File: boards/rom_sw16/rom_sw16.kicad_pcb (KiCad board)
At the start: 2 copper layers, 99.1 x 99.1 mm, 95 parts, among them J1 Conn_02x10_Top_Bottom, SW1 SW_DIP_x08, SW10 SW_DIP_x08, SW11 SW_DIP_x08, SW12 SW_DIP_x08, SW13 SW_DIP_x08, SW14 SW_DIP_x08, SW15 SW_DIP_x08, SW16 SW_DIP_x08, SW2 SW_DIP_x08, SW3 SW_DIP_x08, SW4 SW_DIP_x08, SW5 SW_DIP_x08, SW6 SW_DIP_x08, SW7 SW_DIP_x08, SW8 SW_DIP_x08, SW9 SW_DIP_x08, U1 74HC138, U2 74HC138, U3 74HC240

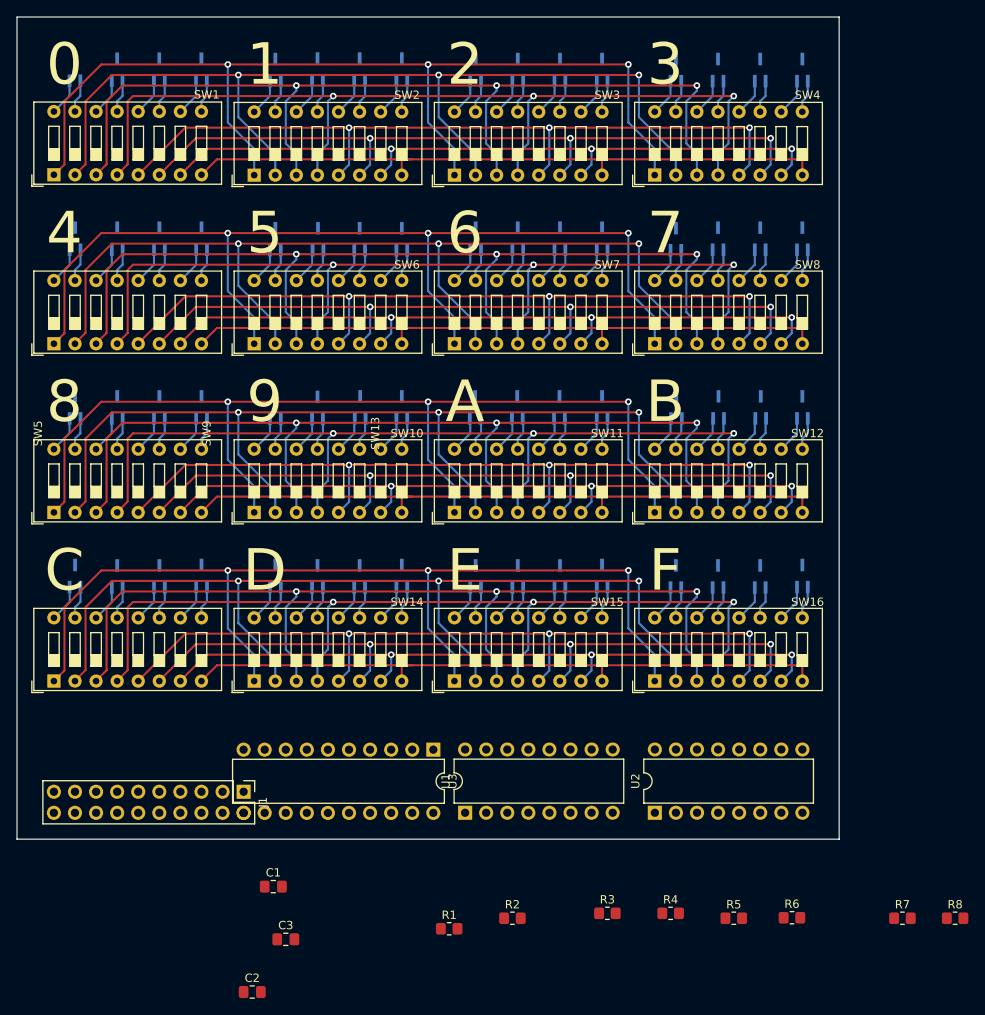
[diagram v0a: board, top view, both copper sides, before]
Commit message: rom_sw16: add board design
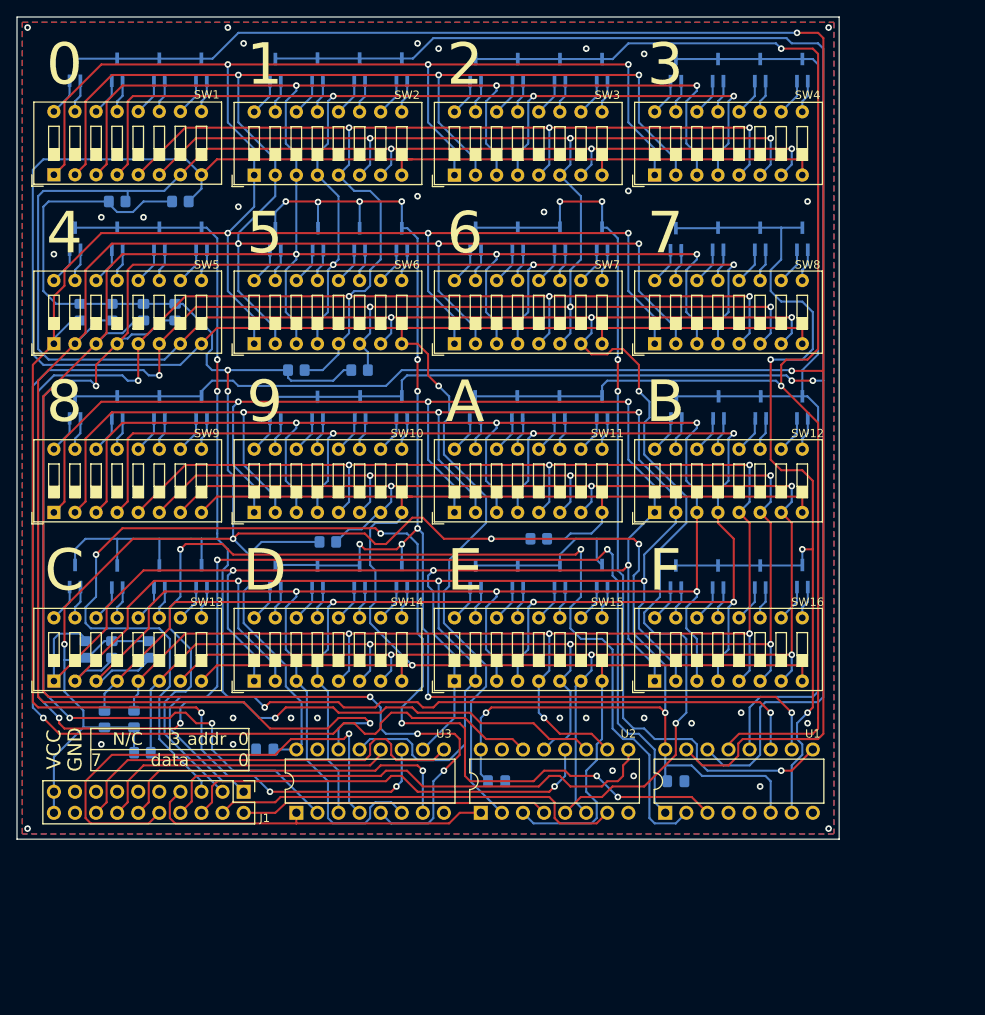
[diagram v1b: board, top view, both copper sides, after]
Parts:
- added R1: 10k, Resistor_SMD:R_0805_2012Metric_Pad1.20x1.40mm_HandSolder, B.Cu at (66.0, 43.8)
- added R10: 10k, Resistor_SMD:R_0805_2012Metric_Pad1.20x1.40mm_HandSolder, B.Cu at (83.8, 84.8)
- added R11: 10k, Resistor_SMD:R_0805_2012Metric_Pad1.20x1.40mm_HandSolder, B.Cu at (61.5, 110.2)
- added R12: 10k, Resistor_SMD:R_0805_2012Metric_Pad1.20x1.40mm_HandSolder, B.Cu at (60.5, 106.2)
- added R2: 10k, Resistor_SMD:R_0805_2012Metric_Pad1.20x1.40mm_HandSolder, B.Cu at (58.4, 43.8)
- added R3: 10k, Resistor_SMD:R_0805_2012Metric_Pad1.20x1.40mm_HandSolder, B.Cu at (87.6, 64.1)
- added R4: 10k, Resistor_SMD:R_0805_2012Metric_Pad1.20x1.40mm_HandSolder, B.Cu at (80.0, 64.1)
- added R9: 10k, Resistor_SMD:R_0805_2012Metric_Pad1.20x1.40mm_HandSolder, B.Cu at (109.2, 84.5)
- C1, C2, C3: moved to B.Cu
- R13: renamed from R2; moved to B.Cu
- R14: renamed from R4; moved to B.Cu
- R15: renamed from R6; moved to B.Cu
- R16: renamed from R8; moved to B.Cu
- R5: renamed from R1; moved to B.Cu
- R6: renamed from R3; moved to B.Cu
- R7: renamed from R5; moved to B.Cu
- R8: renamed from R7; moved to B.Cu
- U2: value 74HC138 -> 74HC158
- U3: value 74HC240 -> 74HC158; footprint PrjLibrary_MainBoard:DIP-20_W7.62mm_D1mm -> PrjLibrary_MainBoard:DIP-16_W7.62mm_D1mm
- moved R8 123.1 mm to (54.0, 57.1), turned to -90 degrees
- moved R16 109.7 mm to (54.6, 97.8), turned to 90 degrees
- moved R7 104.6 mm to (57.8, 57.1), turned to -90 degrees
- moved R6 91.5 mm to (61.6, 57.1), turned to -90 degrees
- moved R15 88.1 mm to (57.8, 97.8), turned to -90 degrees
- moved R5 81.3 mm to (65.4, 57.1), turned to -90 degrees
- moved R14 70.5 mm to (62.2, 97.8), turned to -90 degrees
- moved R13 54.7 mm to (56.9, 106.2), turned to 90 degrees
- moved C1 50.1 mm to (125.7, 113.7)
- moved C2 38.9 mm to (104.1, 113.7)
- moved U1 24.1 mm to (124.5, 117.5)
- moved C3 23.0 mm to (76.2, 109.9), turned to 180 degrees
- moved U2 21.0 mm to (102.2, 117.5)
- moved U3 18.2 mm to (80.0, 117.5), turned to 90 degrees
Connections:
- D33 pad 3: /enB -> /en3
- D34 pad 3: /enB -> /en3
- D35 pad 3: /enB -> /en3
- D36 pad 3: /enB -> /en3
- D37 pad 3: /enA -> /en2
- D38 pad 3: /enA -> /en2
- D39 pad 3: /enA -> /en2
- D40 pad 3: /enA -> /en2
- D41 pad 3: /en9 -> /en1
- D42 pad 3: /en9 -> /en1
- D43 pad 3: /en9 -> /en1
- D44 pad 3: /en9 -> /en1
- D45 pad 3: /en8 -> /en0
- D46 pad 3: /en8 -> /en0
- D47 pad 3: /en8 -> /en0
- D48 pad 3: /en8 -> /en0
- D49 pad 3: /enF -> /en7
- D50 pad 3: /enF -> /en7
- D51 pad 3: /enF -> /en7
- D52 pad 3: /enF -> /en7
- D53 pad 3: /enE -> /en6
- D54 pad 3: /enE -> /en6
- D55 pad 3: /enE -> /en6
- D56 pad 3: /enE -> /en6
- D57 pad 3: /enD -> /en5
- D58 pad 3: /enD -> /en5
- D59 pad 3: /enD -> /en5
- D60 pad 3: /enD -> /en5
- D61 pad 3: /enC -> /en4
- D62 pad 3: /enC -> /en4
- D63 pad 3: /enC -> /en4
- D64 pad 3: /enC -> /en4
- R13 pad 2: /sw1 -> /sH4
- R14 pad 2: /sw3 -> /sH5
- R15 pad 2: /sw5 -> /sH6
- R16 pad 2: /sw7 -> /sH7
- R5 pad 2: /sw0 -> /sL4
- R6 pad 2: /sw2 -> /sL5
- R7 pad 2: /sw4 -> /sL6
- R8 pad 2: /sw6 -> /sL7
- SW1 pad 1: /sw7 -> /sL7
- SW1 pad 2: /sw6 -> /sL6
- SW1 pad 3: /sw5 -> /sL5
- SW1 pad 4: /sw4 -> /sL4
- SW1 pad 5: /sw3 -> /sL3
- SW1 pad 6: /sw2 -> /sL2
- SW1 pad 7: /sw1 -> /sL1
- SW1 pad 8: /sw0 -> /sL0
- SW10 pad 1: /sw7 -> /sH7
- SW10 pad 2: /sw6 -> /sH6
- SW10 pad 3: /sw5 -> /sH5
- SW10 pad 4: /sw4 -> /sH4
- SW10 pad 5: /sw3 -> /sH3
- SW10 pad 6: /sw2 -> /sH2
- SW10 pad 7: /sw1 -> /sH1
- SW10 pad 8: /sw0 -> /sH0
- SW11 pad 1: /sw7 -> /sH7
- SW11 pad 2: /sw6 -> /sH6
- SW11 pad 3: /sw5 -> /sH5
- SW11 pad 4: /sw4 -> /sH4
- SW11 pad 5: /sw3 -> /sH3
- SW11 pad 6: /sw2 -> /sH2
- SW11 pad 7: /sw1 -> /sH1
- SW11 pad 8: /sw0 -> /sH0
- SW12 pad 1: /sw7 -> /sH7
- SW12 pad 2: /sw6 -> /sH6
- SW12 pad 3: /sw5 -> /sH5
- SW12 pad 4: /sw4 -> /sH4
- SW12 pad 5: /sw3 -> /sH3
- SW12 pad 6: /sw2 -> /sH2
- SW12 pad 7: /sw1 -> /sH1
- SW12 pad 8: /sw0 -> /sH0
- SW13 pad 1: /sw7 -> /sH7
- SW13 pad 2: /sw6 -> /sH6
- SW13 pad 3: /sw5 -> /sH5
- SW13 pad 4: /sw4 -> /sH4
- SW13 pad 5: /sw3 -> /sH3
- SW13 pad 6: /sw2 -> /sH2
- SW13 pad 7: /sw1 -> /sH1
- SW13 pad 8: /sw0 -> /sH0
- SW14 pad 1: /sw7 -> /sH7
- SW14 pad 2: /sw6 -> /sH6
- SW14 pad 3: /sw5 -> /sH5
- SW14 pad 4: /sw4 -> /sH4
- SW14 pad 5: /sw3 -> /sH3
- SW14 pad 6: /sw2 -> /sH2
- SW14 pad 7: /sw1 -> /sH1
- SW14 pad 8: /sw0 -> /sH0
- SW15 pad 1: /sw7 -> /sH7
- SW15 pad 2: /sw6 -> /sH6
- SW15 pad 3: /sw5 -> /sH5
- SW15 pad 4: /sw4 -> /sH4
- SW15 pad 5: /sw3 -> /sH3
- SW15 pad 6: /sw2 -> /sH2
- SW15 pad 7: /sw1 -> /sH1
- SW15 pad 8: /sw0 -> /sH0
- SW16 pad 1: /sw7 -> /sH7
- SW16 pad 2: /sw6 -> /sH6
- SW16 pad 3: /sw5 -> /sH5
- SW16 pad 4: /sw4 -> /sH4
- SW16 pad 5: /sw3 -> /sH3
- SW16 pad 6: /sw2 -> /sH2
- SW16 pad 7: /sw1 -> /sH1
- SW16 pad 8: /sw0 -> /sH0
- SW2 pad 1: /sw7 -> /sL7
- SW2 pad 2: /sw6 -> /sL6
- SW2 pad 3: /sw5 -> /sL5
- SW2 pad 4: /sw4 -> /sL4
- SW2 pad 5: /sw3 -> /sL3
- SW2 pad 6: /sw2 -> /sL2
- SW2 pad 7: /sw1 -> /sL1
- SW2 pad 8: /sw0 -> /sL0
- SW3 pad 1: /sw7 -> /sL7
- SW3 pad 2: /sw6 -> /sL6
- SW3 pad 3: /sw5 -> /sL5
- SW3 pad 4: /sw4 -> /sL4
- SW3 pad 5: /sw3 -> /sL3
- SW3 pad 6: /sw2 -> /sL2
- SW3 pad 7: /sw1 -> /sL1
- SW3 pad 8: /sw0 -> /sL0
- SW4 pad 1: /sw7 -> /sL7
- SW4 pad 2: /sw6 -> /sL6
- SW4 pad 3: /sw5 -> /sL5
- SW4 pad 4: /sw4 -> /sL4
- SW4 pad 5: /sw3 -> /sL3
- SW4 pad 6: /sw2 -> /sL2
- SW4 pad 7: /sw1 -> /sL1
- SW4 pad 8: /sw0 -> /sL0
- SW5 pad 1: /sw7 -> /sL7
- SW5 pad 2: /sw6 -> /sL6
- SW5 pad 3: /sw5 -> /sL5
- SW5 pad 4: /sw4 -> /sL4
- SW5 pad 5: /sw3 -> /sL3
- SW5 pad 6: /sw2 -> /sL2
- SW5 pad 7: /sw1 -> /sL1
- SW5 pad 8: /sw0 -> /sL0
- SW6 pad 1: /sw7 -> /sL7
- SW6 pad 2: /sw6 -> /sL6
- SW6 pad 3: /sw5 -> /sL5
- SW6 pad 4: /sw4 -> /sL4
- SW6 pad 5: /sw3 -> /sL3
- SW6 pad 6: /sw2 -> /sL2
- SW6 pad 7: /sw1 -> /sL1
- SW6 pad 8: /sw0 -> /sL0
- SW7 pad 1: /sw7 -> /sL7
- SW7 pad 2: /sw6 -> /sL6
- SW7 pad 3: /sw5 -> /sL5
- SW7 pad 4: /sw4 -> /sL4
- SW7 pad 5: /sw3 -> /sL3
- SW7 pad 6: /sw2 -> /sL2
- SW7 pad 7: /sw1 -> /sL1
- SW7 pad 8: /sw0 -> /sL0
- SW8 pad 1: /sw7 -> /sL7
- SW8 pad 2: /sw6 -> /sL6
- SW8 pad 3: /sw5 -> /sL5
- SW8 pad 4: /sw4 -> /sL4
- SW8 pad 5: /sw3 -> /sL3
- SW8 pad 6: /sw2 -> /sL2
- SW8 pad 7: /sw1 -> /sL1
- SW8 pad 8: /sw0 -> /sL0
- SW9 pad 1: /sw7 -> /sH7
- SW9 pad 2: /sw6 -> /sH6
- SW9 pad 3: /sw5 -> /sH5
- SW9 pad 4: /sw4 -> /sH4
- SW9 pad 5: /sw3 -> /sH3
- SW9 pad 6: /sw2 -> /sH2
- SW9 pad 7: /sw1 -> /sH1
- SW9 pad 8: /sw0 -> /sH0
- U1 pad 5: /addr3 -> GND
- U2 pad 1: /addr0 -> /addr3
- U2 pad 10: /enD -> /sH3
- U2 pad 11: /enC -> /sL3
- U2 pad 12: /enB -> /data2
- U2 pad 13: /enA -> /sH2
- U2 pad 14: /en9 -> /sL2
- U2 pad 15: /en8 -> GND
- U2 pad 2: /addr1 -> /sL0
- U2 pad 3: /addr2 -> /sH0
- U2 pad 4: GND -> /data0
- U2 pad 5: GND -> /sL1
- U2 pad 6: /addr3 -> /sH1
- U2 pad 7: /enF -> /data1
- U2 pad 9: /enE -> /data3
- U3 pad 1: GND -> /addr3
- U3 pad 10: GND -> /sH7
- U3 pad 11: /sw7 -> /sL7
- U3 pad 12: /data3 -> /data6
- U3 pad 13: /sw6 -> /sH6
- U3 pad 14: /data2 -> /sL6
- U3 pad 15: /sw5 -> GND
- U3 pad 16: /data1 -> VCC
- U3 pad 2: /sw0 -> /sL4
- U3 pad 3: /data4 -> /sH4
- U3 pad 4: /sw1 -> /data4
- U3 pad 5: /data5 -> /sL5
- U3 pad 6: /sw2 -> /sH5
- U3 pad 7: /data6 -> /data5
- U3 pad 8: /sw3 -> GND
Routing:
- net /sw7: track 492.5 -> 0.00 mm, vias 12 -> 0
- net /sw6: track 476.3 -> 0.00 mm, vias 12 -> 0
- net /sw5: track 467.3 -> 0.00 mm, vias 12 -> 0
- net /sw4: track 454.4 -> 0.00 mm, vias 12 -> 0
- net /sw3: track 378.9 -> 0.00 mm, vias 12 -> 0
- net /sL5: track 0.00 -> 366.6 mm, vias 0 -> 9
- net /sw2: track 361.6 -> 0.00 mm, vias 12 -> 0
- net /sL7: track 0.00 -> 359.4 mm, vias 0 -> 9
- net /sL6: track 0.00 -> 347.2 mm, vias 0 -> 7
- net /sL3: track 0.00 -> 344.5 mm, vias 0 -> 10
- net /sw1: track 344.2 -> 0.00 mm, vias 12 -> 0
- net VCC: track 0.00 -> 342.0 mm, vias 0 -> 8
- net /sL4: track 0.00 -> 338.0 mm, vias 0 -> 9
- net /sL2: track 0.00 -> 325.4 mm, vias 0 -> 8
- net /sw0: track 320.6 -> 0.00 mm
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- added copper zone on B.Cu, net GND
- added copper zone on F.Cu, net GND
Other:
- board text added: "16-Octet Switch ROM Board v1.0"
- board text added: "GND"
- board text added: "N/C"
- board text added: "VCC"
- board text added: "addr"
- board text added: "data"

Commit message: unify libraries
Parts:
- J1: footprint PrjLibrary_MainBoard:PinHeader_2x10_P2.54mm_Vertical_Top_Bottom -> ModifiedKiCadLibrary:PinHeader_2x10_P2.54mm_Vertical_Top_Bottom
- SW1, SW10, SW11, SW12, SW13, SW14, SW15, SW16, SW2, SW3, SW4, SW5, SW6, SW7, SW8, SW9: footprint PrjLibrary:SW_DIP_SPSTx08_Slide_9.78x22.5mm_W7.62mm_P2.54mm_3Dfixed -> ModifiedKiCadLibrary:SW_DIP_SPSTx08_Slide_9.78x22.5mm_W7.62mm_P2.54mm_3Dfixed
- U1, U2, U3: footprint PrjLibrary_MainBoard:DIP-16_W7.62mm_D1mm -> ModifiedKiCadLibrary:DIP-16_W7.62mm_D1mm
